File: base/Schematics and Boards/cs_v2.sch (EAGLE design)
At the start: 4 parts, among them U1 ATSAMD51

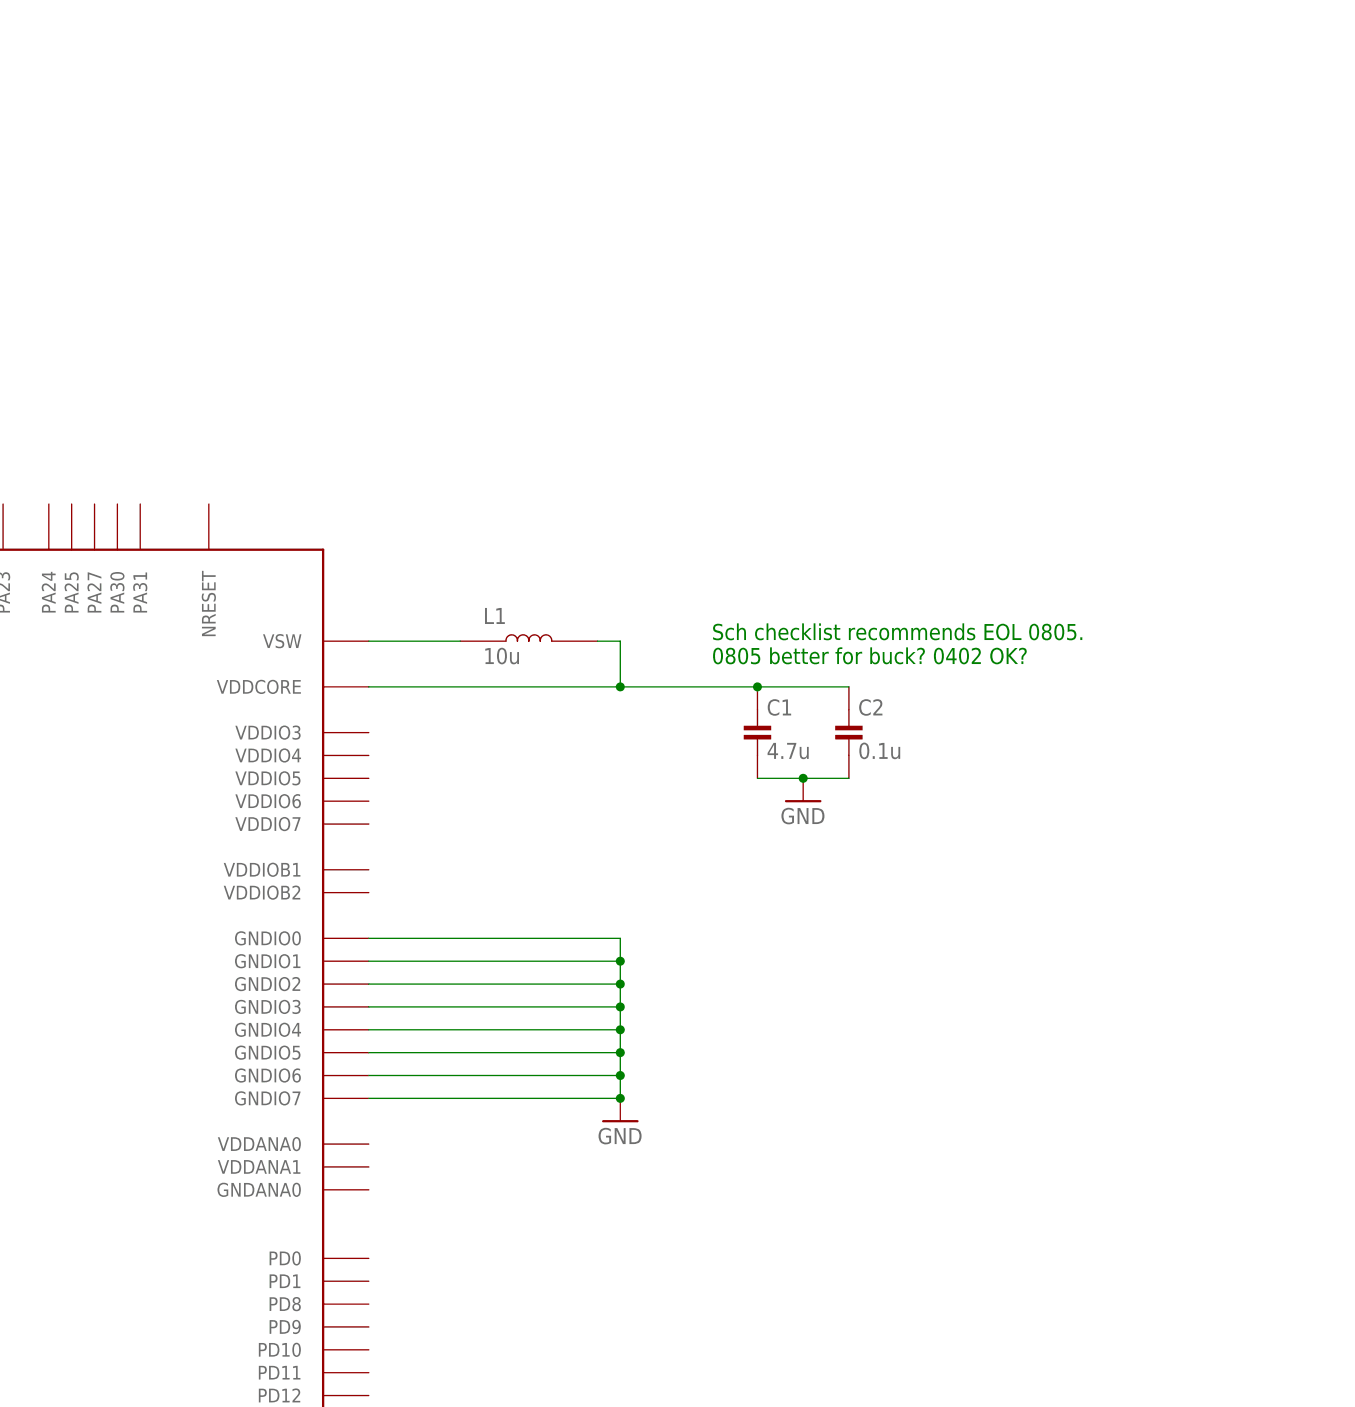
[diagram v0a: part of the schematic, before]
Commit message: Add caps for D51 power pins; add reset sw
Added all necessary caps and inductors for the power connection of the processor. 

Also added the reset switch. Using a switch from the sparkfun libraries. Part was chosen based on size.

All added parts are included with part numbers from Kemet (C), Panasonic (R), or whichever brand Atmel recommends (mostly for inductors)
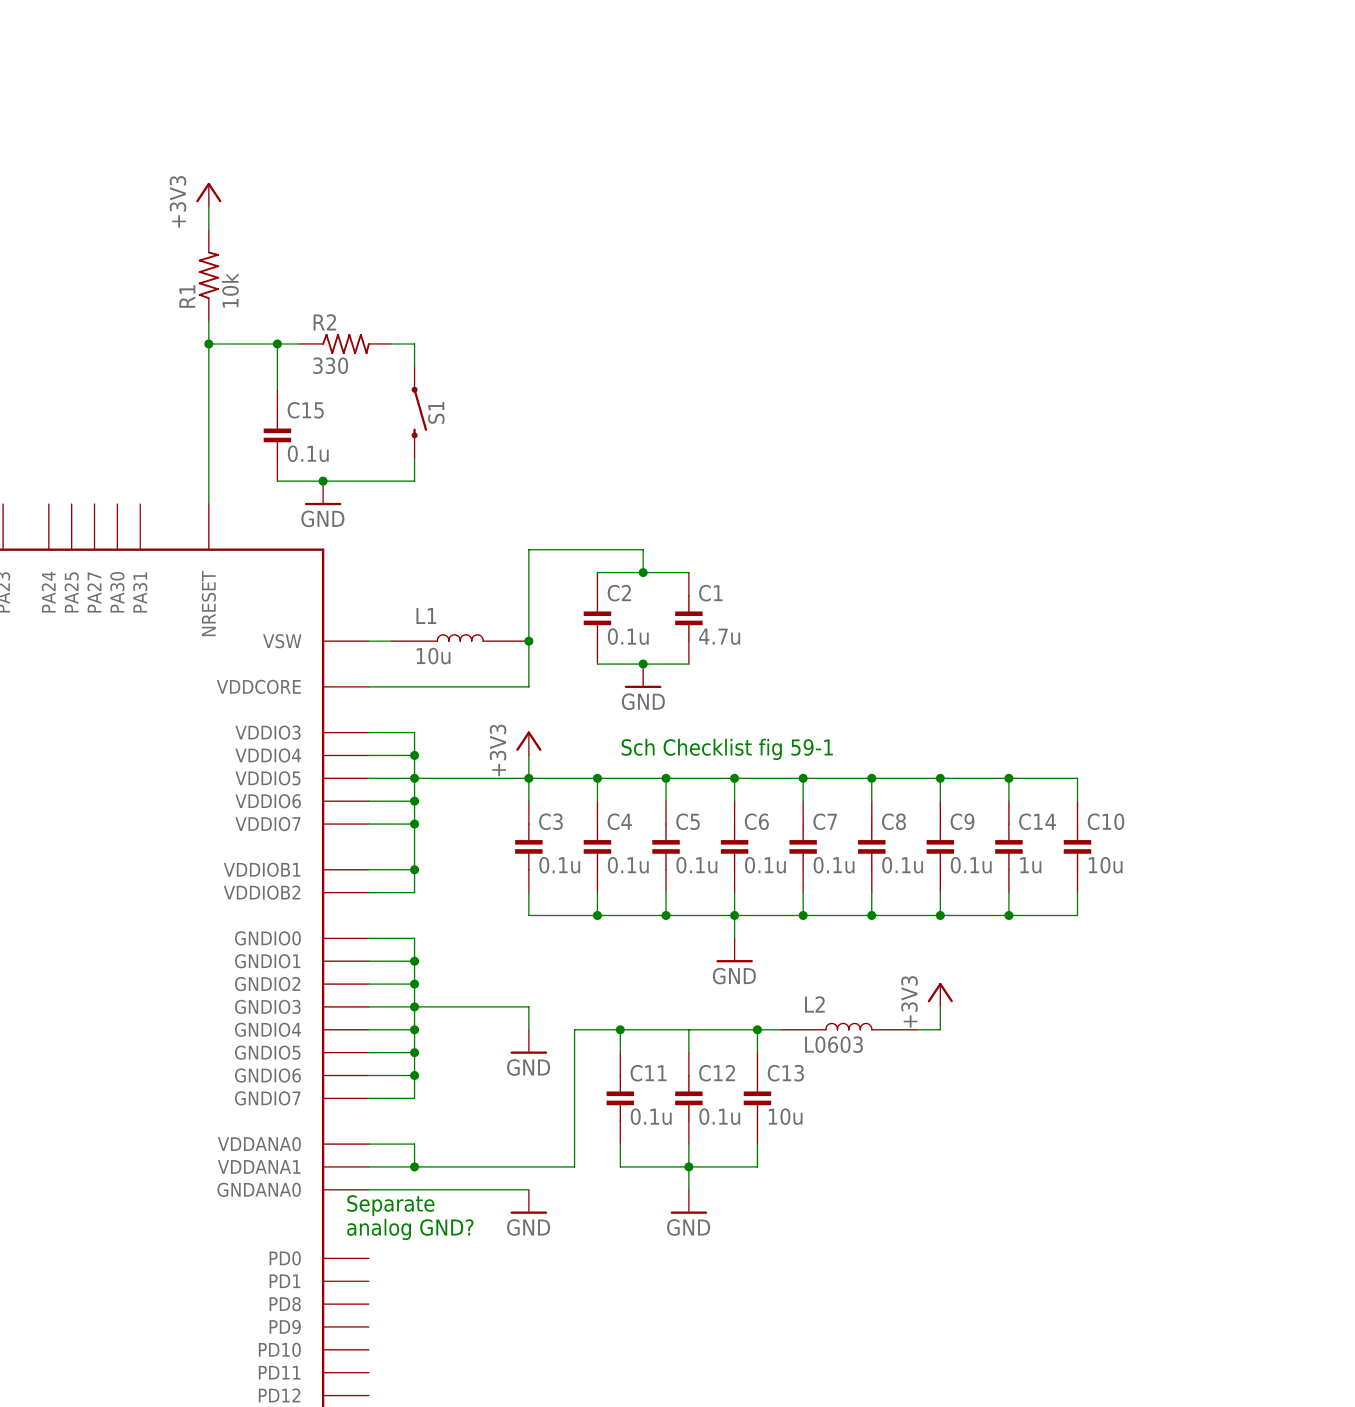
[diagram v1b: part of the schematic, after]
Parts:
- added C10, C13: 10u, Capacitors:C-0805
- added C11, C12, C15, C3, C4, C5, C6, C7, C8, C9: 0.1u, Capacitors:C-0402
- added C14: 1u, Capacitors:C-0603
- added L2: L0603, Inductors:L0603
- added R1: 10k, Resistors:R-0402
- added R2: 330, Resistors:R-0402
- added S1: MOMENTARY-SWITCH-SPST-SMD-4.6X2.8MM, SparkFun-Switches:MOMENTARY-SWITCH-SPST-SMD-4.6X2.8MM
- C1: device Capacitors:C-0402 -> Capacitors:C-0805; PART_NO (none) -> C0805C475K8RACTU; VOLTAGE (none) -> 10V
- C2: PART_NO (none) -> C0402C104K8RACTU; VOLTAGE (none) -> 10V
- L1: PART_NO (none) -> LQH3NPN100NM0L
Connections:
- new net +3V3: C10.1, C14.1, C3.1, C4.1, C5.1, C6.1, C7.1, C8.1, C9.1, L2.2, R1.2, U1.VDDIO3, U1.VDDIO4, U1.VDDIO5, U1.VDDIO6, U1.VDDIO7, U1.VDDIOB1, U1.VDDIOB2
- new net GND1: C11.2, C12.2, C13.2
- new net N$3: C11.1, C12.1, C13.1, L2.1, U1.VDDANA0, U1.VDDANA1
- new net N$5: R2.2, S1.1
- new net N$6: C15.1, R1.1, R2.1, U1.NRESET
- net GND: now also C10.2, C14.2, C15.2, C3.2, C4.2, C5.2, C6.2, C7.2, C8.2, C9.2, S1.2, U1.GNDANA0
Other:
- note added: "Sch Checklist fig 59-1"
- note added: "Separate analog GND?"
- note removed: "Sch checklist recommends EOL 0805. 0805 better for buck? 0402 OK?"
- moved on the sheet: C1, C2, L1

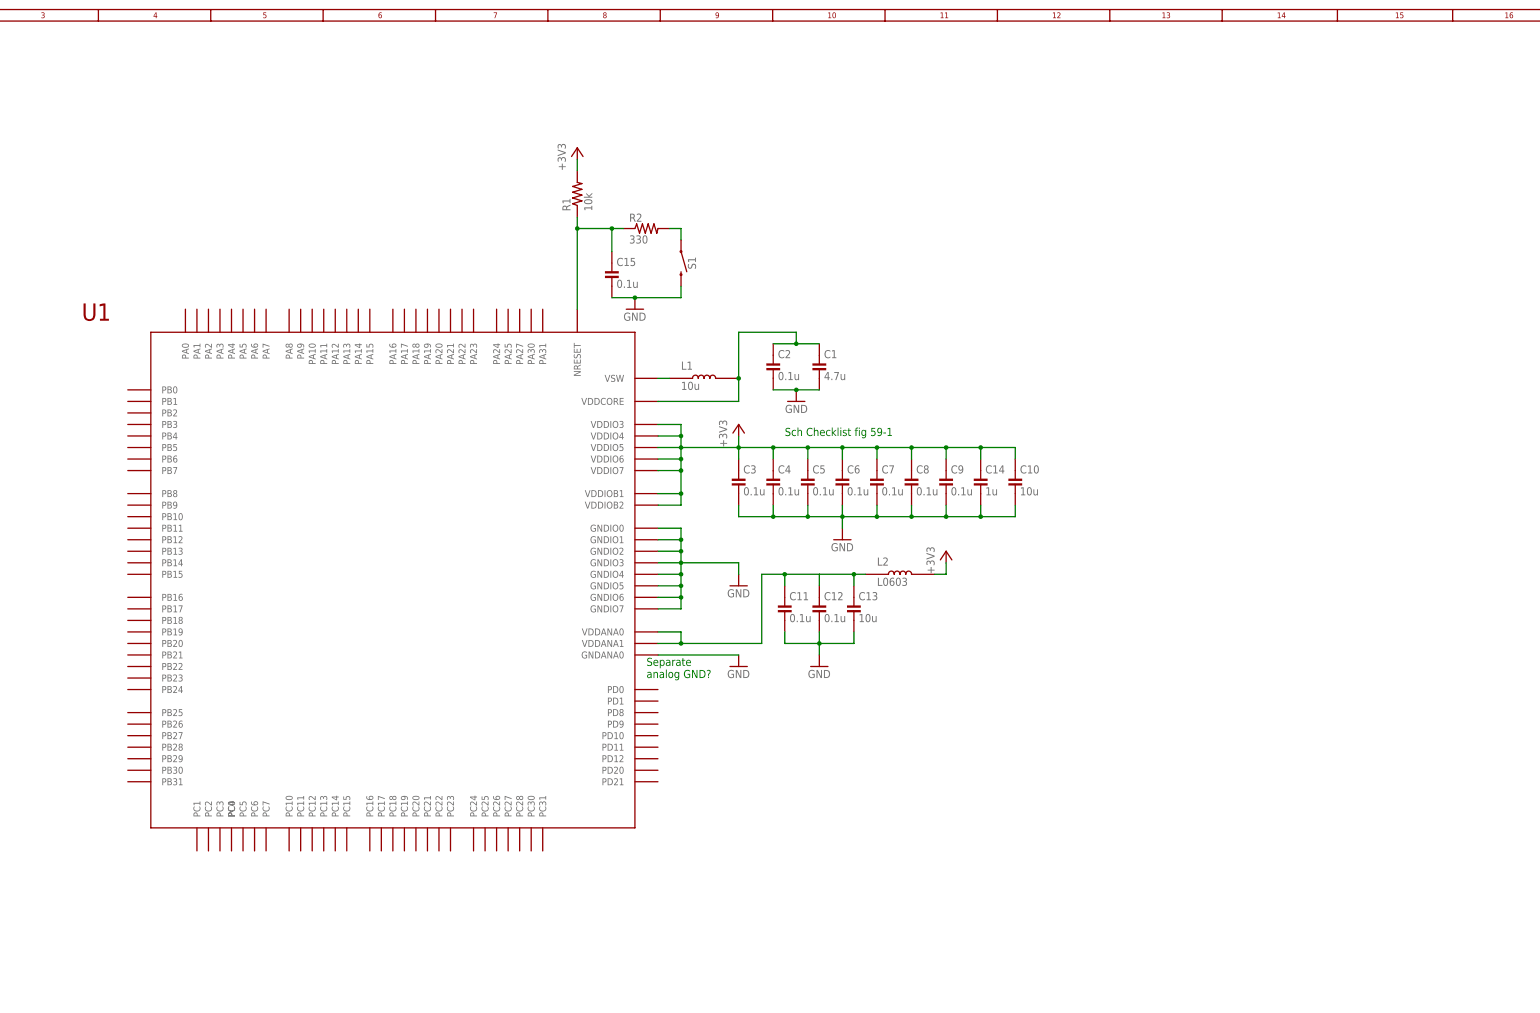
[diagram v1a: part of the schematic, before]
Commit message: Start adding xtals. Loads not calculated, fast xtal added
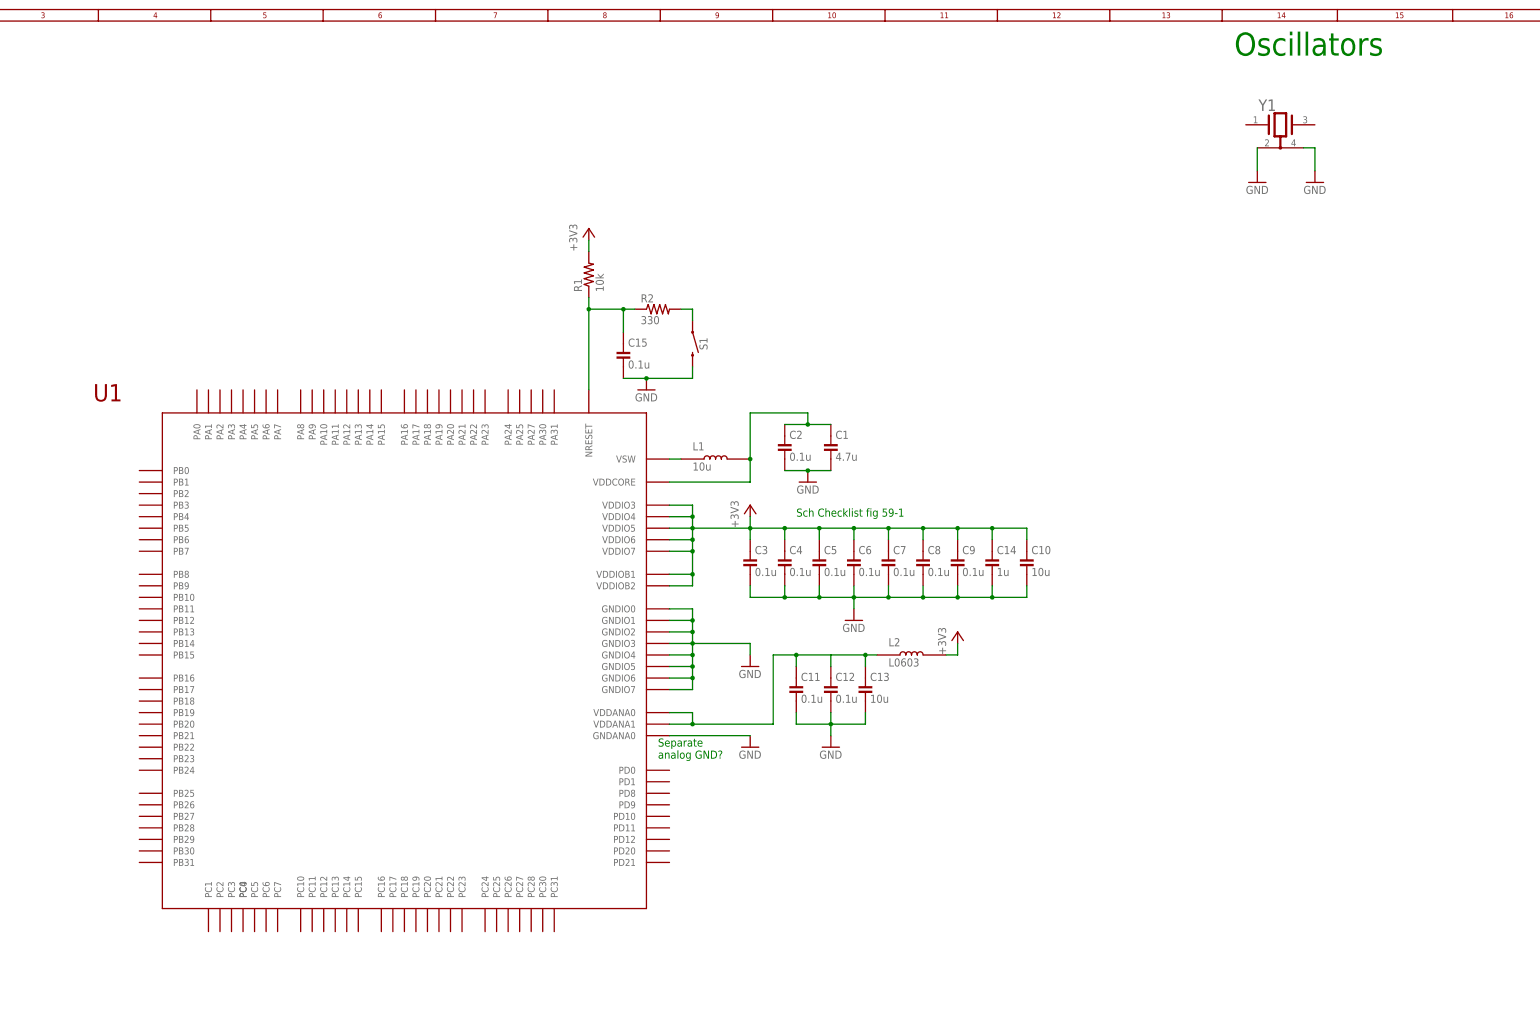
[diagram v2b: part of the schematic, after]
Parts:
- added Y1: TSX-3225_16.0000MF09Z-AC3, Oscillators:TSX-3225_16.0000MF09Z-AC3
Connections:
- net GND: now also Y1.1_GND, Y1.2_GND
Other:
- note added: "Oscillators"
- moved on the sheet: C1, C10, C11, C12, C13, C14, C15, C2, C3, C4, C5, C6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
